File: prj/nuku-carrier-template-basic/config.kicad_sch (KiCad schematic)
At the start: 8 parts, among them SW2 RESET, U5 IS25LP064A, U6 OT3225100MJBA4SL

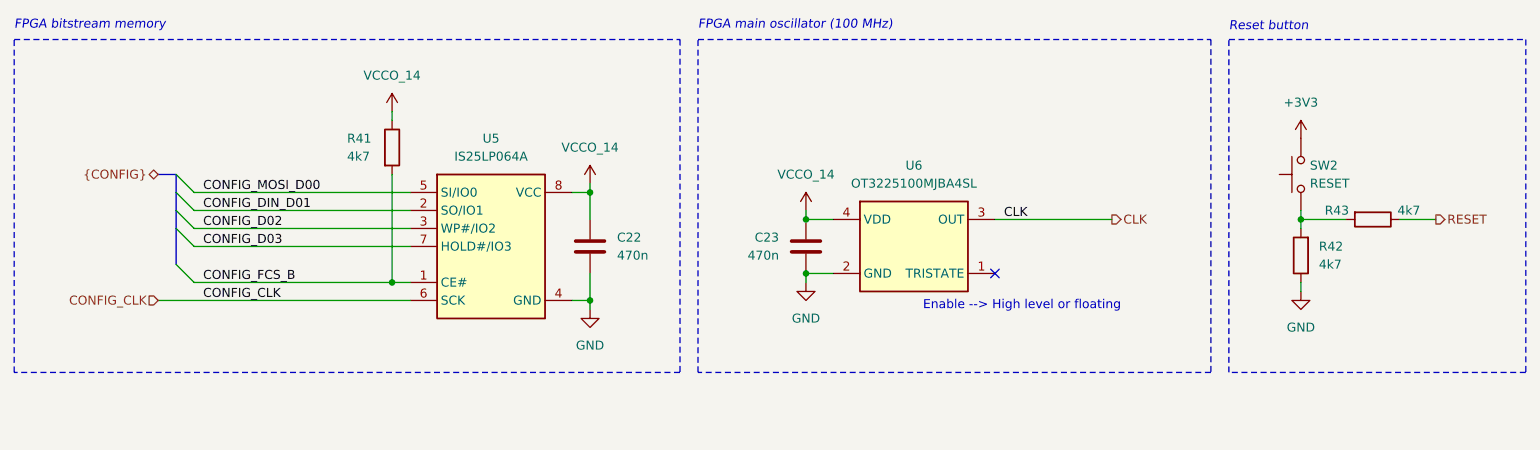
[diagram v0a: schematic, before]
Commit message: Finish template.basic + Production outputs
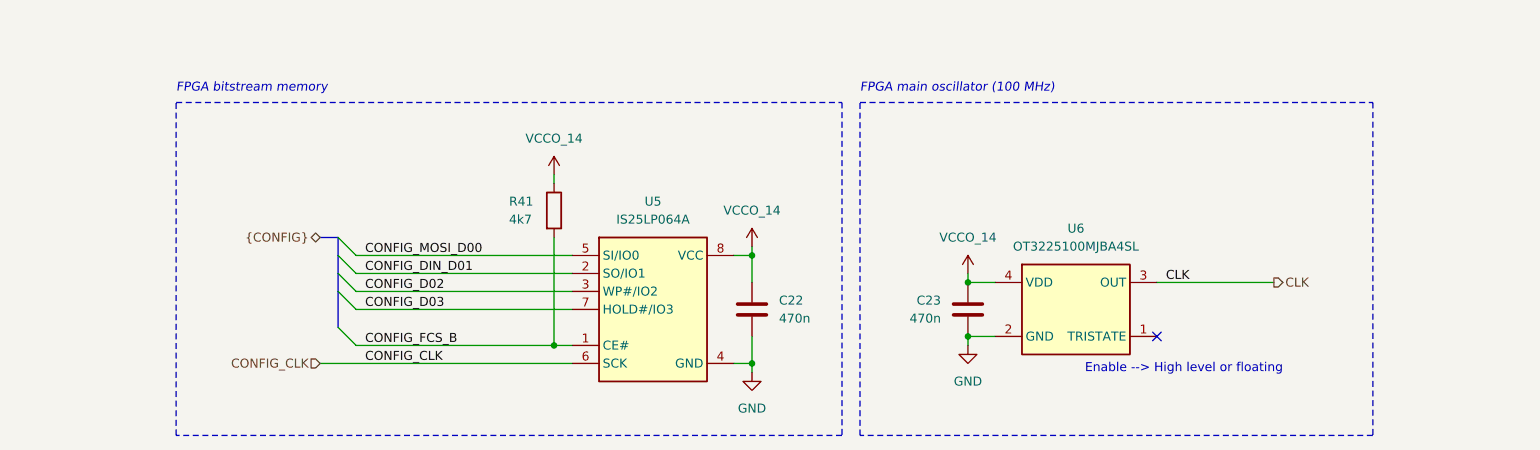
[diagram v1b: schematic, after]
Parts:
- removed R42, R43: 4k7, Resistor_SMD:R_0402_1005Metric, symbol Device:R
- removed SW2: RESET, nuku:TS-1088-AR02016, symbol Switch:SW_Push
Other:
- note removed: "Reset button"
- moved on the sheet: C22, C23, R41, U5, U6
